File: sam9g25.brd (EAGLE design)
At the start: 65 x 46 mm, 131 parts, among them IC1 AT91SAM9G25, IC3 LAN8710, IC4 NCP1529, IC5 NCP1529, IC6 NCP1529, IC7 H5PSXG63JFR, Q1 12MHz, X2 USB-A-HU, X3 MICRO-SD_MOLEX-502774-001, X4 HFJ11-2450E

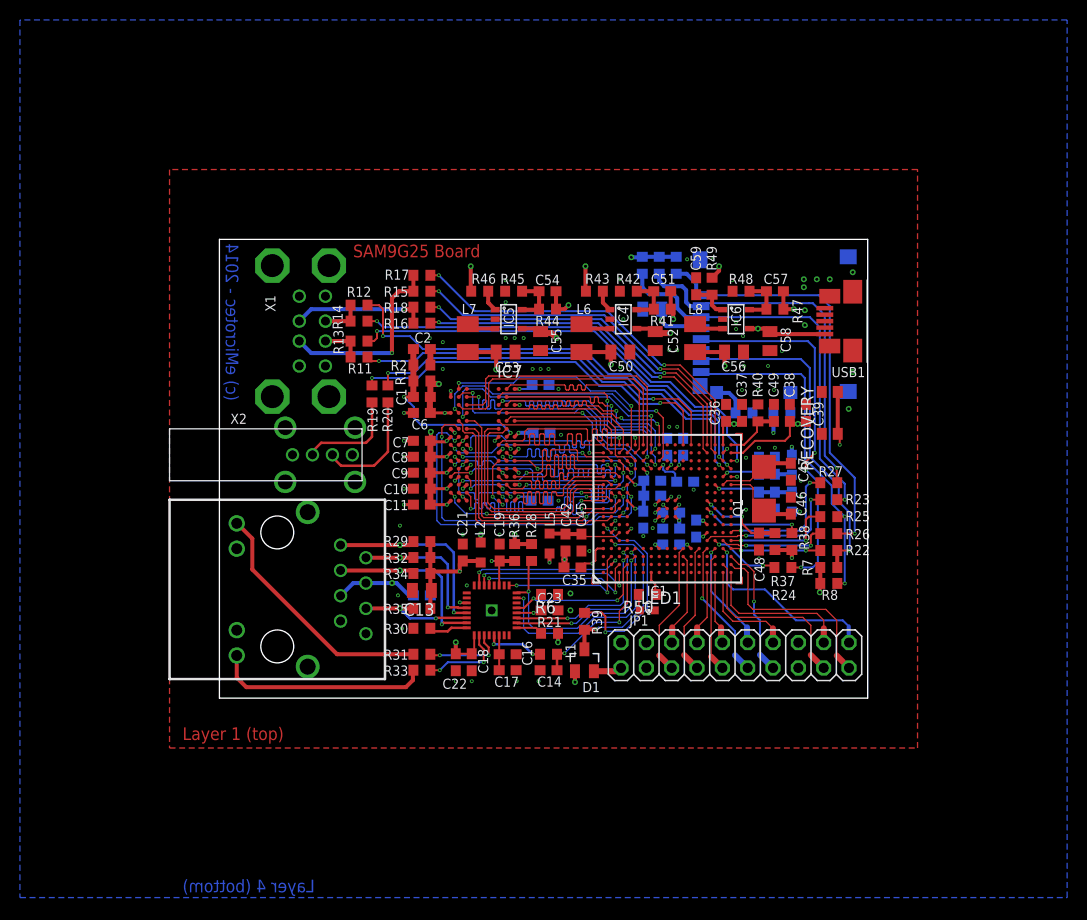
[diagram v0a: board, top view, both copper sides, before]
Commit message: Fixed ethernet refclk hardware bug Fixed usb ports
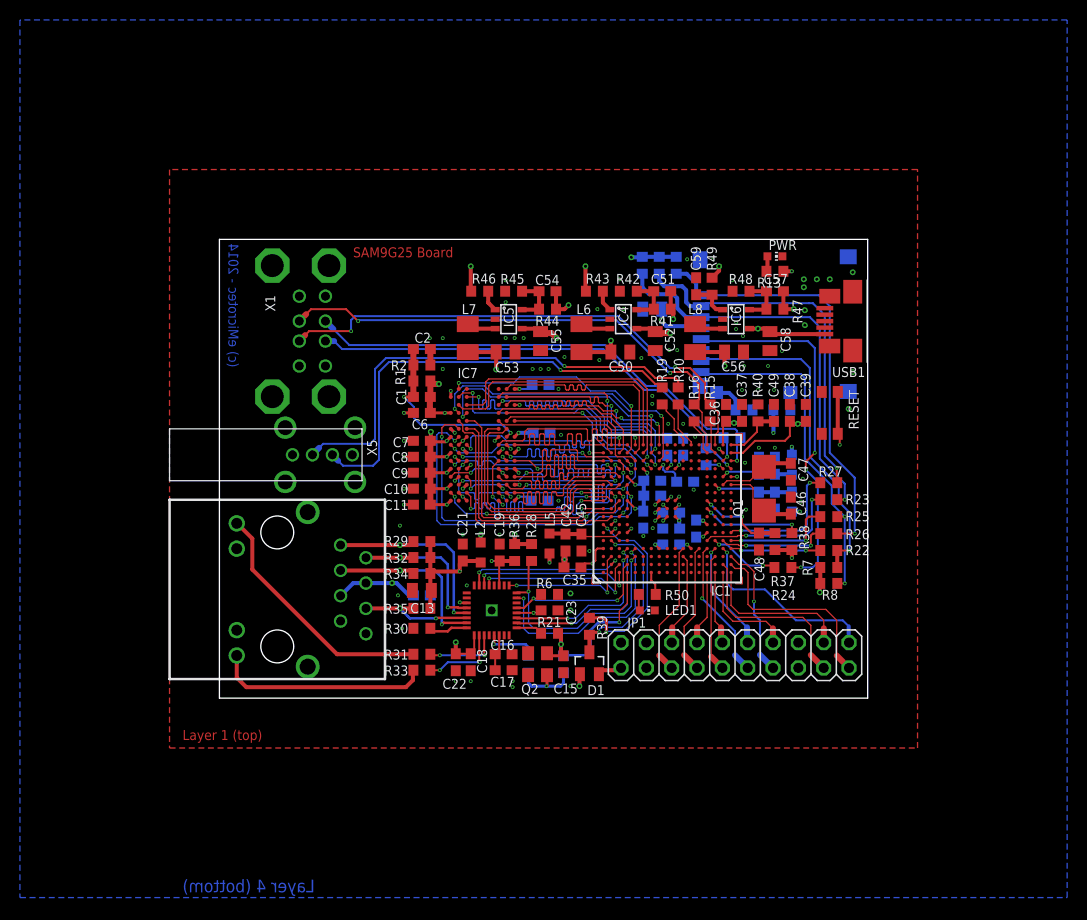
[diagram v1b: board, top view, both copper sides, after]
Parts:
- removed C14: 27p, rcl:C0603
- removed L1: 120@100MHz, mystuff:0603
- removed R14, R17, R18: 0, rcl:R0603
- removed X2: USB-A-HU, mystuff:USB-A-HU
- added C15: 1u, rcl:C0603
- added PWR: (no value), led:CHIP-LED0603
- added Q2: SI50X, myrf:DFN4
- added R51, R52: 27, rcl:R0603
- added X5: USB-A-HU, mycon:USB-A-HU
- C12, C13: value 22uF/6.3V -> 22u/6.3V
- C50, C53, C56: value 10u/6V3 -> 22u/6V3
- R1, R2: value 1k5 -> 1k
- R13: value 0 -> 1k
- R29, R32, R34, R35: value 51R -> 49R9
- R36: value 12k1 -> 10k
- R50: value 1k -> 470R
- moved R13 42.3 mm to (55.7, 42.8)
- moved R12 39.7 mm to (51.4, 26.1), flipped to the bottom
- moved R11 36.2 mm to (48.8, 24.2), flipped to the bottom, turned to 90 degrees
- moved R15 31.4 mm to (49.2, 28.6), turned to 90 degrees
- moved R20 29.1 mm to (46.0, 30.3), turned to 90 degrees
- moved R19 29.1 mm to (44.4, 30.3), turned to 90 degrees
- moved R16 28.7 mm to (47.6, 28.6), turned to 90 degrees
- moved R39 0.71 mm to (37.1, 7.20)
- moved D1 0.58 mm to (37.1, 3.50)
- moved C16 0.40 mm to (28.5, 4.40)
- moved C17 0.40 mm to (28.5, 2.80)
- moved R10 0.30 mm to (52.6, 28.9)
- moved R9 0.30 mm to (56.4, 28.9)
- moved C18 0.10 mm to (25.2, 3.60)
- renumbered RECOVERY to RESET
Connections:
- net N$10 renamed HFSDMB
- net N$15 renamed HFSDPC
- net N$16 renamed HFSDMC
- net N$3 renamed HFSDPA
- net N$4 renamed HFSDMA
- net N$9 renamed HFSDPB
- removed net N$11: R15.2, R17.2, X1.B3
- removed net N$12: R16.2, R18.2, X1.B2
- removed net N$13: IC1.R17, R17.1
- removed net N$14: IC1.P17, R18.1
- removed net N$5: IC1.U14, R13.1
- removed net N$6: IC1.U15, R14.1
- removed net N$7: R11.2, R13.2, X1.A3
- removed net N$8: R12.2, R14.2, X1.A2
- new net HHSDMA: IC1.U15, R12.2, X1.A2
- new net HHSDMB: IC1.P17, R16.2, X1.B2
- new net HHSDPA: IC1.U14, R11.2, X1.A3
- new net HHSDPB: IC1.R17, R15.2, X1.B3
- new net N$4: PWR.A, R13.2
- new net N$46: Q2.3, R51.1, R52.2
- net +3V3: now also C15.1, Q2.4, R13.1
- net +5V: now also X5.VBUS; no longer X2.VBUS
- net ETH_CLK: now also R52.1; no longer C14.1, L1.1
- net GND: now also C15.2, PWR.C, Q2.2, X5.GND; no longer C14.2, X2.GND
- net N$17: now also X5.D+; no longer X2.D+
- net N$18: now also X5.D-; no longer X2.D-
- net N$2: now also R51.2; no longer L1.2
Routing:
- net HHSDPB: track 0.00 -> 52.1 mm, vias 0 -> 2
- net HHSDMB: track 0.00 -> 50.7 mm, vias 0 -> 2
- net HHSDMA: track 0.00 -> 49.9 mm, vias 0 -> 1
- net HHSDPA: track 0.00 -> 46.8 mm, vias 0 -> 1
- net N$5: track 45.4 -> 0.00 mm, vias 2 -> 0
- net N$6: track 45.4 -> 0.00 mm, vias 2 -> 0
- net HFSDMA: track 45.7 -> 2.61 mm, vias 2 -> 1
- net HFSDPA: track 43.1 -> 1.89 mm, vias 2 -> 1
- net N$13: track 38.2 -> 0.00 mm, vias 2 -> 0
- net N$14: track 35.9 -> 0.00 mm, vias 2 -> 0
- net N$18: track 11.7 -> 46.4 mm, vias 0 -> 1
- net HFSDPB: track 38.0 -> 3.36 mm, vias 2 -> 0
- net N$17: track 10.4 -> 44.2 mm, vias 0 -> 1
- net HFSDMC: track 37.8 -> 4.59 mm, vias 2 -> 0
- net HFSDPC: track 38.1 -> 4.92 mm, vias 2 -> 0
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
